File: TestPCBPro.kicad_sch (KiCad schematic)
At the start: 0 parts

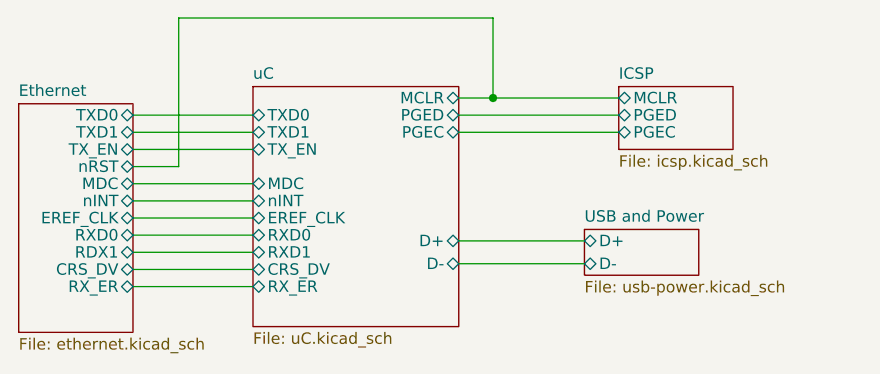
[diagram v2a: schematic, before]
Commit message: Added connection for MDIO to the PIC Complete redesign of board, reduced size from 100x50 to 75x35mm Readded C15 and C16 to the front Added some test points
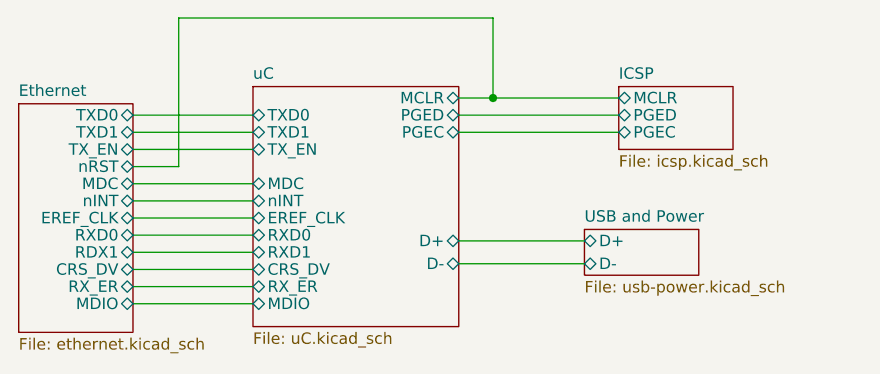
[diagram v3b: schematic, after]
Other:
- sheet Ethernet ports: added MDIO; removed none
- sheet uC ports: added MDIO; removed none
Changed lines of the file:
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@@
+    (stroke (width 0) (type default) (color 0 0 0 0))
+  )
+  (wire (pts (xy 112.395 128.27) (xy 125.73 128.27))
     (stroke (width 0) (type default) (color 0 0 0 0))
   )
@@
       (effects (font (size 1.27 1.27)) (justify right))
     )
+    (pin "MDIO" bidirectional (at 112.395 128.27 0)
+      (effects (font (size 1.27 1.27)) (justify right))
+    )
   )
   (sheet (at 125.73 104.14) (size 22.86 26.67) (fields_autoplaced)
@@
     )
     (pin "CRS_DV" bidirectional (at 125.73 124.46 180)
+      (effects (font (size 1.27 1.27)) (justify left))
+    )
+    (pin "MDIO" bidirectional (at 125.73 128.27 180)
       (effects (font (size 1.27 1.27)) (justify left))
     )
@@
       (reference "#PWR0157") (unit 1) (value "GND") (footprint "")
     )
-    (path "/44137c28-2258-47a5-b635-260660b262fa/68331111-3d3c-4f02-890f-975371174738"
+    (path "/44137c28-2258-47a5-b635-260660b262fa/d312c0f2-9b73-4011-af94-ea1864805c4f"
       (reference "#PWR0158") (unit 1) (value "+3V3") (footprint "")
     )
@@
       (reference "#PWR0162") (unit 1) (value "VDDA") (footprint "")
     )
-    (path "/44137c28-2258-47a5-b635-260660b262fa/78acec26-d903-4621-be90-8ac90744f5c7"
-      (reference "#PWR0163") (unit 1) (value "+3V3") (footprint "")
-    )
     (path "/44137c28-2258-47a5-b635-260660b262fa/2661f98d-9edc-4487-b234-a0273f10ca14"
       (reference "#PWR0164") (unit 1) (value "GND") (footprint "")
@@
       (reference "R13") (unit 1) (value "10K") (footprint "Lambley:0603-1608M")
     )
-    (path "/44137c28-2258-47a5-b635-260660b262fa/bc0f0ad0-f7be-4b0e-acac-434c4f78932b"
-      (reference "R14") (unit 1) (value "0-DNP") (footprint "Lambley:0603-1608M")
-    )
     (path "/44137c28-2258-47a5-b635-260660b262fa/36087877-8ccf-43f0-bce6-5b2e201bfe1b"
